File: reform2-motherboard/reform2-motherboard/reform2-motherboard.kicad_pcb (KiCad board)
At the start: 6 copper layers, 276 x 93.5 mm, 434 parts, among them J1 Jack-DC, J10 1-2199230-6, J11 48099-5701, J12 BATCON1, J13 BATCON2, J14 USB_INT2, J15 Conn_01x33, J16 LINE_IN, J17 USB3_A, J18 Conn_01x03_Male, J19 JTAG, J2 EDP_30, J20 Conn_01x03_Male, J21 Conn_01x04_Male, J22 LPC_IO, J3 SD_Card, J4 HDMI_A, J5 USB3_A, J6 USB3_A, J7 SJ-43516-SMT, J8 USB_B_Micro, J9 USB_INT1, P1 J0G-0003NL, Q1 Si4850BDY, Q10 PMV50EPEAR, Q11 PMV50EPEAR, Q12 PMV50EPEAR, Q13 PMV55ENEA, Q2 Si4850BDY, Q3 PMV55ENEA, Q4 PMV55ENEA, Q5 PMV50EPEAR, Q6 PMV50EPEAR, Q7 PMV50EPEAR, Q8 PMV50EPEAR, Q9 PMV50EPEAR, SW1 SW_Push, SW2 SW_Push, SW3 SW_DIP_x01, SW6 SW_Push, U1 Nitrogen8M, U10 SN65DSI86ZQER, U11 679105700, U12 LM2677-3.3, U13 TLV71312PDBV, U14 TLV71311PDBV, U15 TPS2561, U16 TPS2561, U17 TLV1117-18, U18 LPC11U24FBD48-301, U19 TLV1117-15, U2 LTC4162-F, U20 WM8731, U21 MAX9715ETE+, U22 CM2020-00TR, U3 LTC4359-MS8, U4 LTC6803-4, U5 LTC4359-MS8, U6 INA260, U7 LM2596T-5, U8 LM2596T-ADJ, U9 TUSB8041, Y1 24MHz, Y2 12MHz

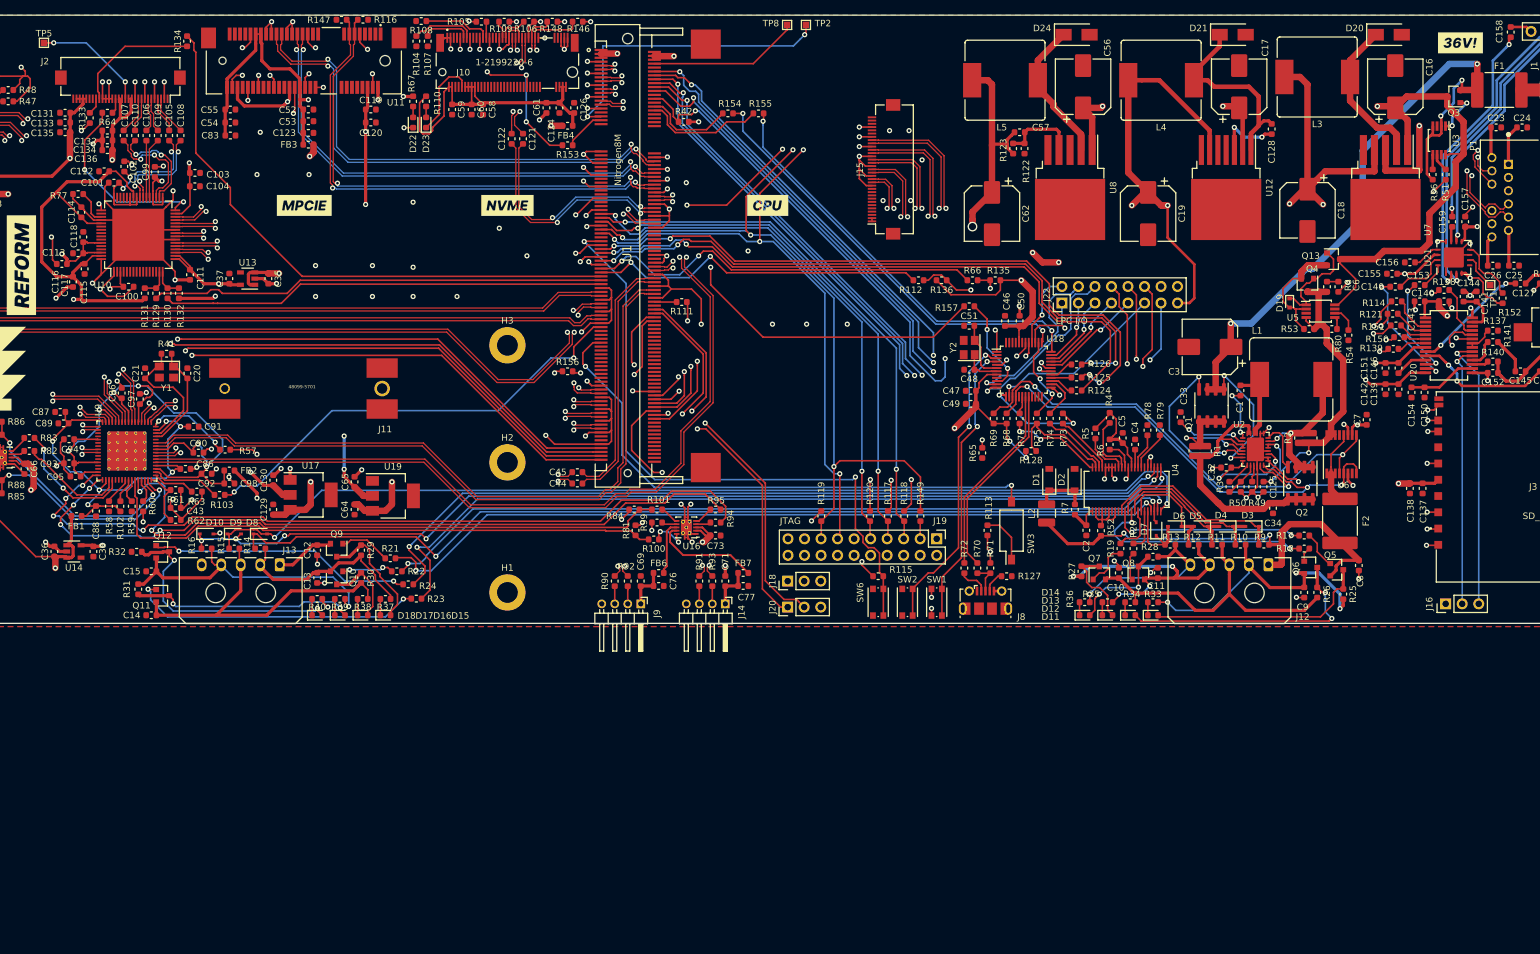
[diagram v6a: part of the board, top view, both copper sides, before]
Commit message: reform2 motherboard: pinout and footprint checks completed; ERC checks fixed 100%
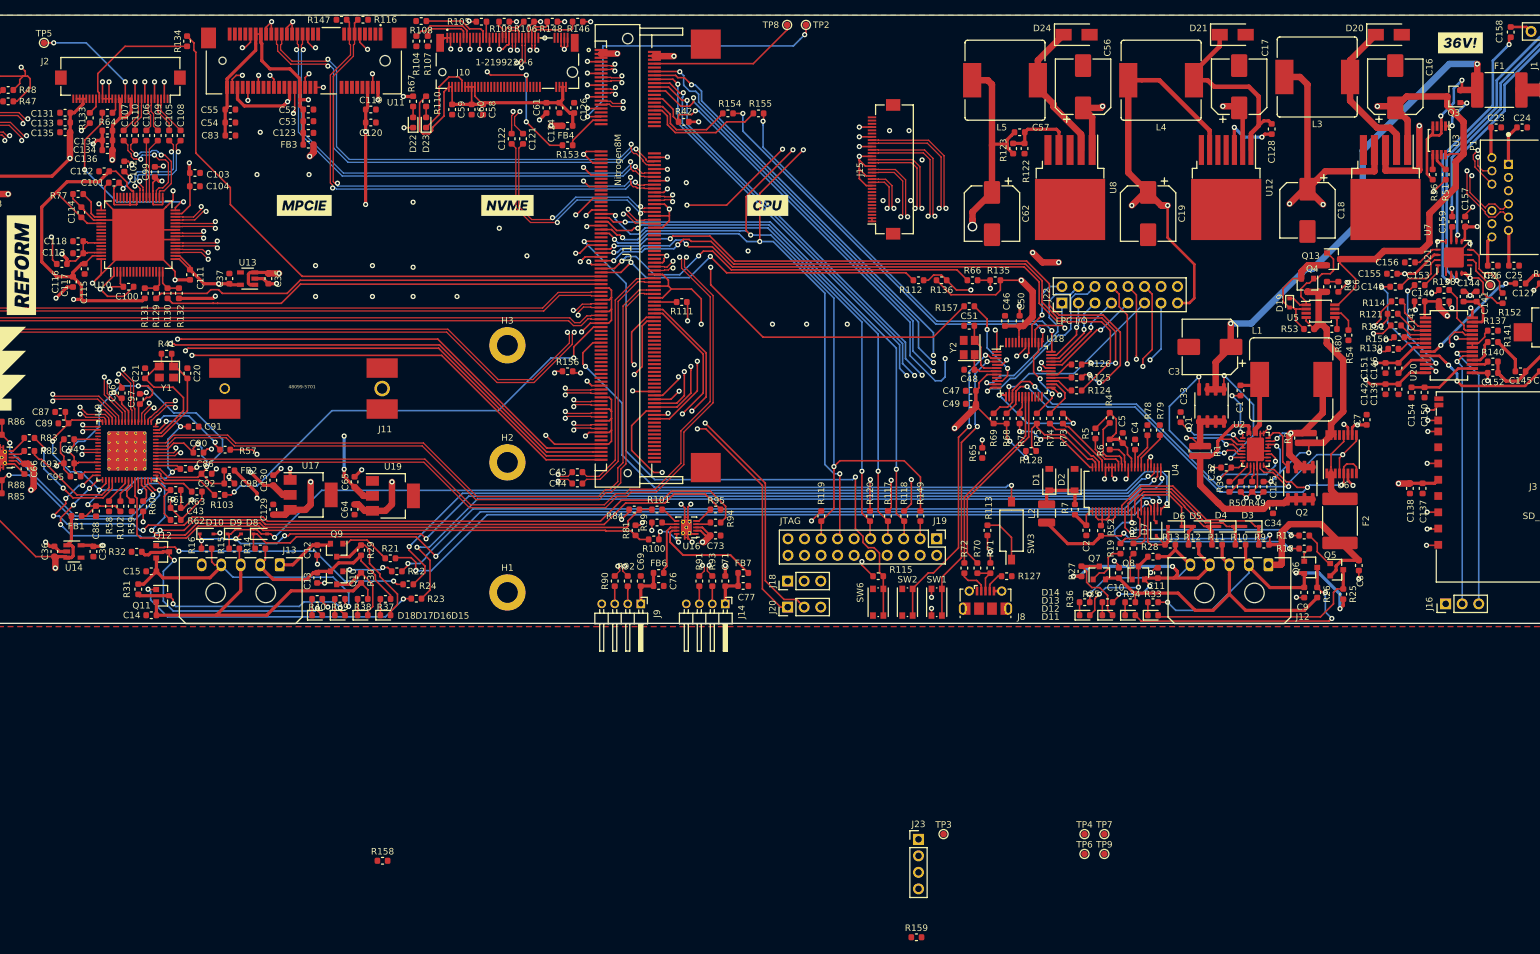
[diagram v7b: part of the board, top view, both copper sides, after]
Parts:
- added J23: POWERS, Connector_PinHeader_2.54mm:PinHeader_1x04_P2.54mm_Vertical, F.Cu at (205.7, 166.7)
- added R158: 0, Resistor_SMD:R_0603_1608Metric, F.Cu at (123.3, 170.0)
- added R159: 0, Resistor_SMD:R_0603_1608Metric, F.Cu at (205.4, 181.8)
- added TP3: T_CHGALERT, TestPoint:TestPoint_Pad_D1.0mm, F.Cu at (209.6, 165.9)
- added TP4: T_EGPIO1, TestPoint:TestPoint_Pad_D1.0mm, F.Cu at (231.2, 165.9)
- added TP6: T_EGPIO2, TestPoint:TestPoint_Pad_D1.0mm, F.Cu at (231.2, 168.9)
- added TP7: T_EGPIO3, TestPoint:TestPoint_Pad_D1.0mm, F.Cu at (234.3, 165.9)
- added TP9: T_EGPIO4, TestPoint:TestPoint_Pad_D1.0mm, F.Cu at (234.3, 168.9)
- R81, R84, R85, R86: value 10k -> 100k
- TP1, TP2, TP5, TP8: footprint TestPoint:TestPoint_Pad_1.0x1.0mm -> TestPoint:TestPoint_Pad_D1.0mm
- U10: value SN65DSI86ZQER -> SN65DSI86IPAPQ1
- moved C118 1.03 mm to (76.5, 74.8), turned to 180 degrees
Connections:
- net /Reform 2 Power/LPC_NCTS renamed /Reform 2 Power/LPC_~CTS
- net /Reform 2 Power/LPC_NDTR renamed /Reform 2 Power/LPC_~DTR
- net /Reform 2 Power/LPC_NRESET renamed /Reform 2 Power/LPC_~RESET
- net /Reform 2 Power/LPC_NUSBCON renamed /Reform 2 Power/LPC_~USBCON
- net /Reform 2 Power/LPC_SCLKb renamed /Reform 2 Power/LPC_PIO1_24
- net /Reform 2 Power/LPC_TRST renamed /Reform 2 Power/LPC_~TRST
- J4 pad 10: HDMI_D3+ -> HDMI_CLK+
- J4 pad 12: HDMI_D3- -> HDMI_CLK-
- U1 pad 163: HDMI_D3+ -> HDMI_CLK-
- U1 pad 165: HDMI_D3- -> HDMI_CLK+
- U2 pad 12: GND -> Net-(TP3-Pad1)
- U2 pad 15: GND -> +3V3
- U22 pad 13: HDMI_D3+ -> HDMI_CLK+
- U22 pad 15: HDMI_D3- -> HDMI_CLK-
- U22 pad 24: HDMI_D3- -> HDMI_CLK-
- U22 pad 26: HDMI_D3+ -> HDMI_CLK+
- U7 pad 5: GND -> ~ON~_USB
- U7 pad 6: (no net) -> GND
- U8 pad 5: GND -> ~ON~_SOM
- U8 pad 6: (no net) -> GND
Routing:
- net HDMI_D3-: track 127.5 -> 0.00 mm, vias 2 -> 0
- net HDMI_D3+: track 126.0 -> 0.00 mm, vias 2 -> 0
- net HDMI_CLK-: track 0.00 -> 125.8 mm, vias 0 -> 2
- net HDMI_CLK+: track 0.00 -> 125.8 mm, vias 0 -> 2
- net GND: track 564.6 -> 558.1 mm, vias 157 -> 156
